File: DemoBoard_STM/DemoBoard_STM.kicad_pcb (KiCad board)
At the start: 4 copper layers, 45 x 45 mm, 57 parts, among them J1 USB4110GFA, J6 M55-7101242R, J7 MSD-1-A, J8 Conn_01x17_Pin, SW1 SW_Push, SW2 SW_Push, U1 RP2040, U2 W25Q128JVSIM, U3 MCP2518FDT-E_QBB, U4 TCAN332DCNR, U5 TLV75533PDBVR, Y1 ABM8-272-T3, Y2 ABM8-20.000MHZ-10-B1U-T

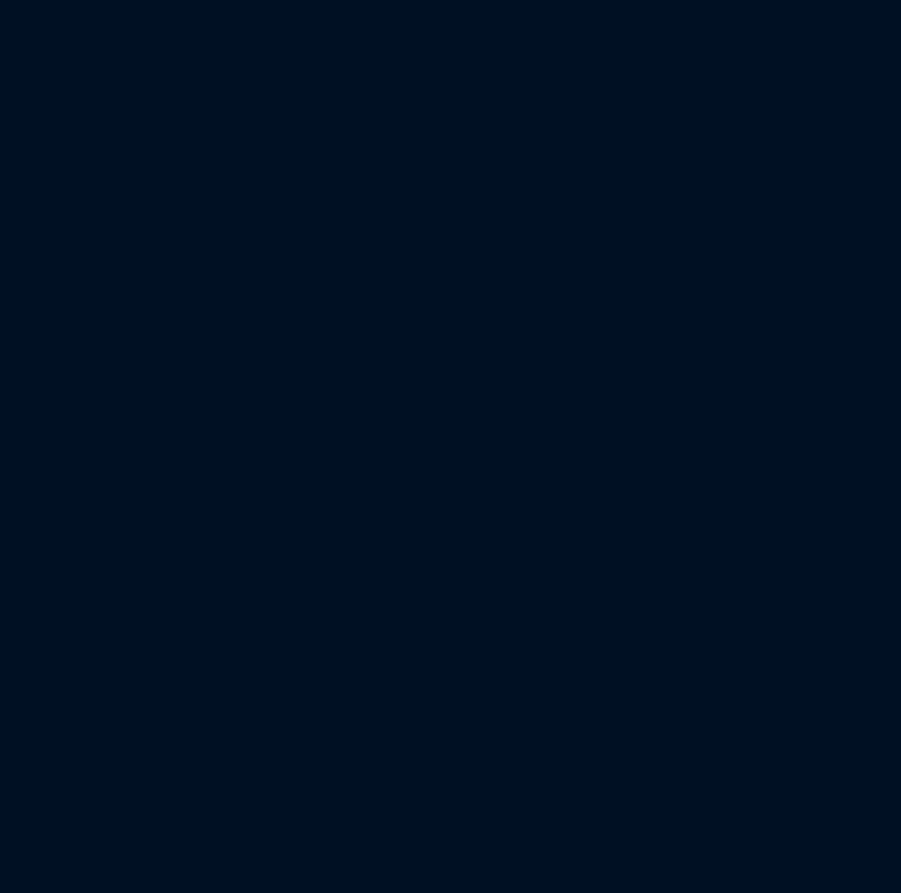
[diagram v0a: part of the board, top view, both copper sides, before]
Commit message: schematic_added_flash
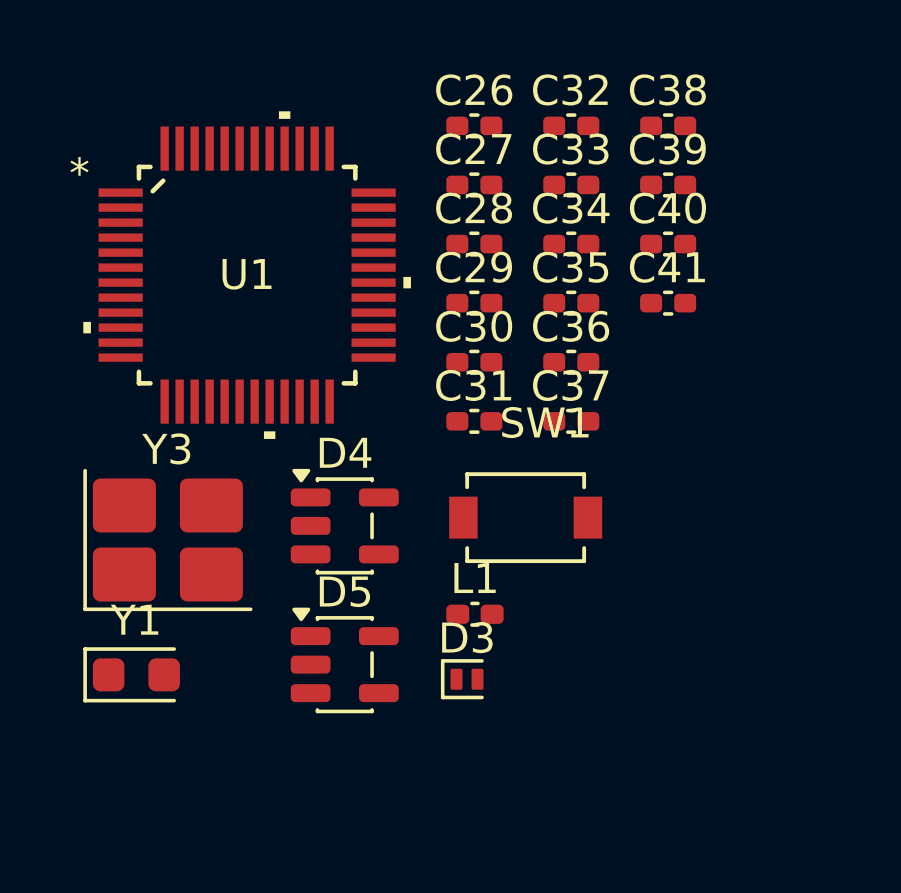
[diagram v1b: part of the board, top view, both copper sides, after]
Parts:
- added C26: 1uF, Capacitor_SMD:C_0402_1005Metric_Pad0.74x0.62mm_HandSolder, F.Cu at (13.0, 0.48)
- added C27: 100nF, Capacitor_SMD:C_0402_1005Metric_Pad0.74x0.62mm_HandSolder, F.Cu at (13.0, 2.46)
- added C28: 100nF, Capacitor_SMD:C_0402_1005Metric_Pad0.74x0.62mm_HandSolder, F.Cu at (13.0, 4.42)
- added C29: 100nF, Capacitor_SMD:C_0402_1005Metric_Pad0.74x0.62mm_HandSolder, F.Cu at (13.0, 6.39)
- added C30: 10uF, Capacitor_SMD:C_0402_1005Metric_Pad0.74x0.62mm_HandSolder, F.Cu at (13.0, 8.37)
- added C31: 100nF, Capacitor_SMD:C_0402_1005Metric_Pad0.74x0.62mm_HandSolder, F.Cu at (13.0, 10.3)
- added C32: 10uF, Capacitor_SMD:C_0402_1005Metric_Pad0.74x0.62mm_HandSolder, F.Cu at (16.3, 0.48)
- added C33: 2.2uF, Capacitor_SMD:C_0402_1005Metric_Pad0.74x0.62mm_HandSolder, F.Cu at (16.3, 2.46)
- added C34: 2.2uF, Capacitor_SMD:C_0402_1005Metric_Pad0.74x0.62mm_HandSolder, F.Cu at (16.3, 4.42)
- added C35: 6.8pF, Capacitor_SMD:C_0402_1005Metric_Pad0.74x0.62mm_HandSolder, F.Cu at (16.3, 6.39)
- added C36: 6.8pF, Capacitor_SMD:C_0402_1005Metric_Pad0.74x0.62mm_HandSolder, F.Cu at (16.3, 8.37)
- added C37: 12pF, Capacitor_SMD:C_0402_1005Metric_Pad0.74x0.62mm_HandSolder, F.Cu at (16.3, 10.3)
- added C38: 12pF, Capacitor_SMD:C_0402_1005Metric_Pad0.74x0.62mm_HandSolder, F.Cu at (19.5, 0.48)
- added C39: 100nF, Capacitor_SMD:C_0402_1005Metric_Pad0.74x0.62mm_HandSolder, F.Cu at (19.5, 2.46)
- added C40: 1uF, Capacitor_SMD:C_0402_1005Metric_Pad0.74x0.62mm_HandSolder, F.Cu at (19.5, 4.42)
- added C41: 100nF, Capacitor_SMD:C_0402_1005Metric_Pad0.74x0.62mm_HandSolder, F.Cu at (19.5, 6.39)
- added D3: PESD3V3U1UL, Diode_SMD:D_SOD-882, F.Cu at (12.8, 18.9)
- added D4: ESDA14V2SC5, Package_TO_SOT_SMD:SOT-23-5, F.Cu at (8.71, 13.8)
- added D5: ESDA14V2SC5, Package_TO_SOT_SMD:SOT-23-5, F.Cu at (8.71, 18.4)
- added L1: 2.2uH, Inductor_SMD:L_0402_1005Metric_Pad0.77x0.64mm_HandSolder, F.Cu at (13.1, 16.8)
- added SW1: SW_Push, inspireFly:SW_TL1015AF160QG, F.Cu at (14.7, 13.5)
- added U1: STM32U375CGT6Q, inspireFly:LQFP48_STM, F.Cu at (5.46, 5.46)
- added Y1: 32.768kHz, Crystal:Crystal_SMD_2012-2Pin_2.0x1.2mm_HandSoldering, F.Cu at (1.77, 18.8)
- added Y3: 16MHz, Crystal:Crystal_SMD_3225-4Pin_3.2x2.5mm_HandSoldering, F.Cu at (2.82, 14.3)

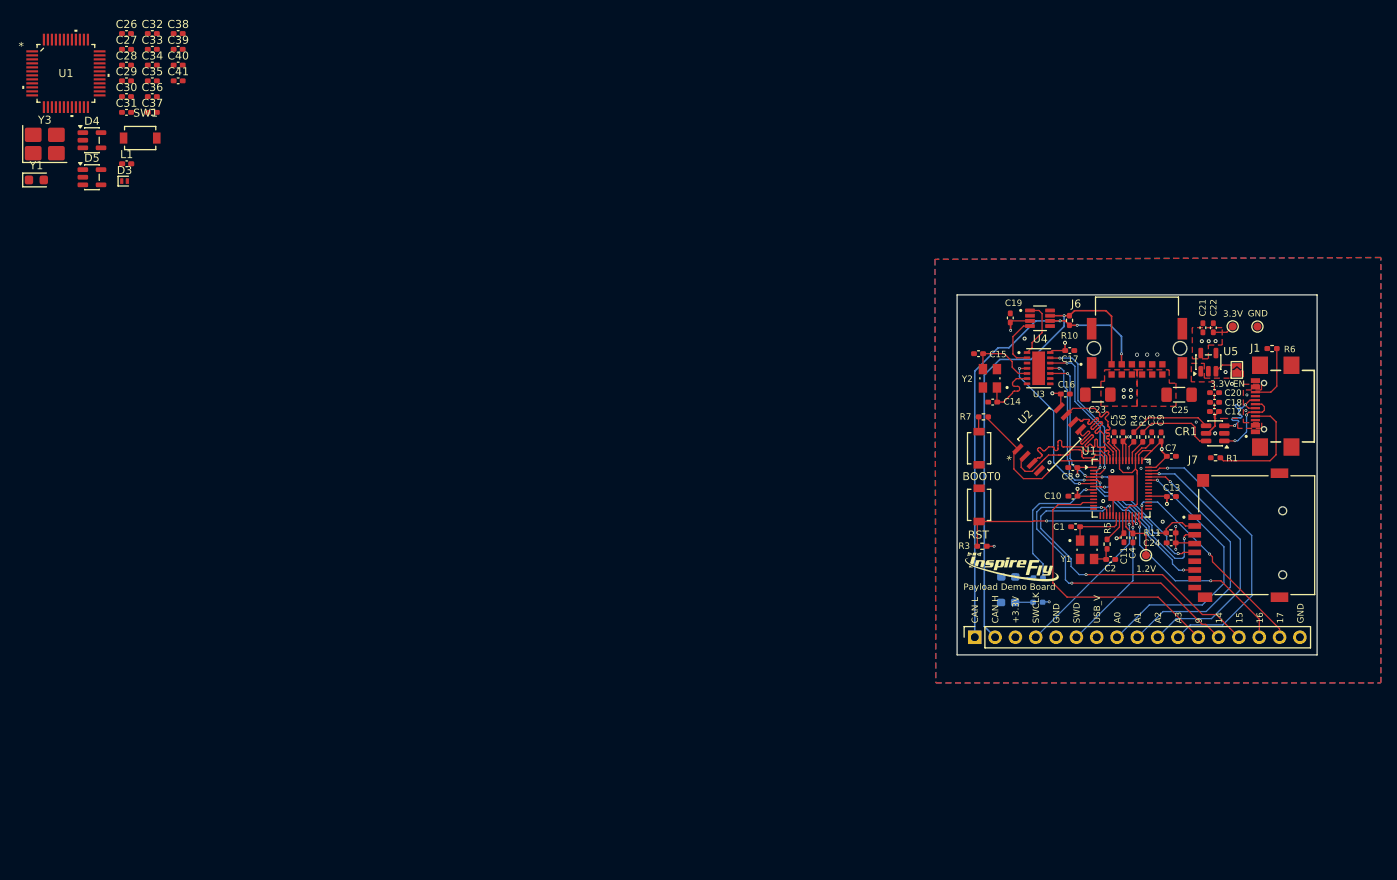
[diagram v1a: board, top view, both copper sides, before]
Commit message: Routing + schematic updates for STM
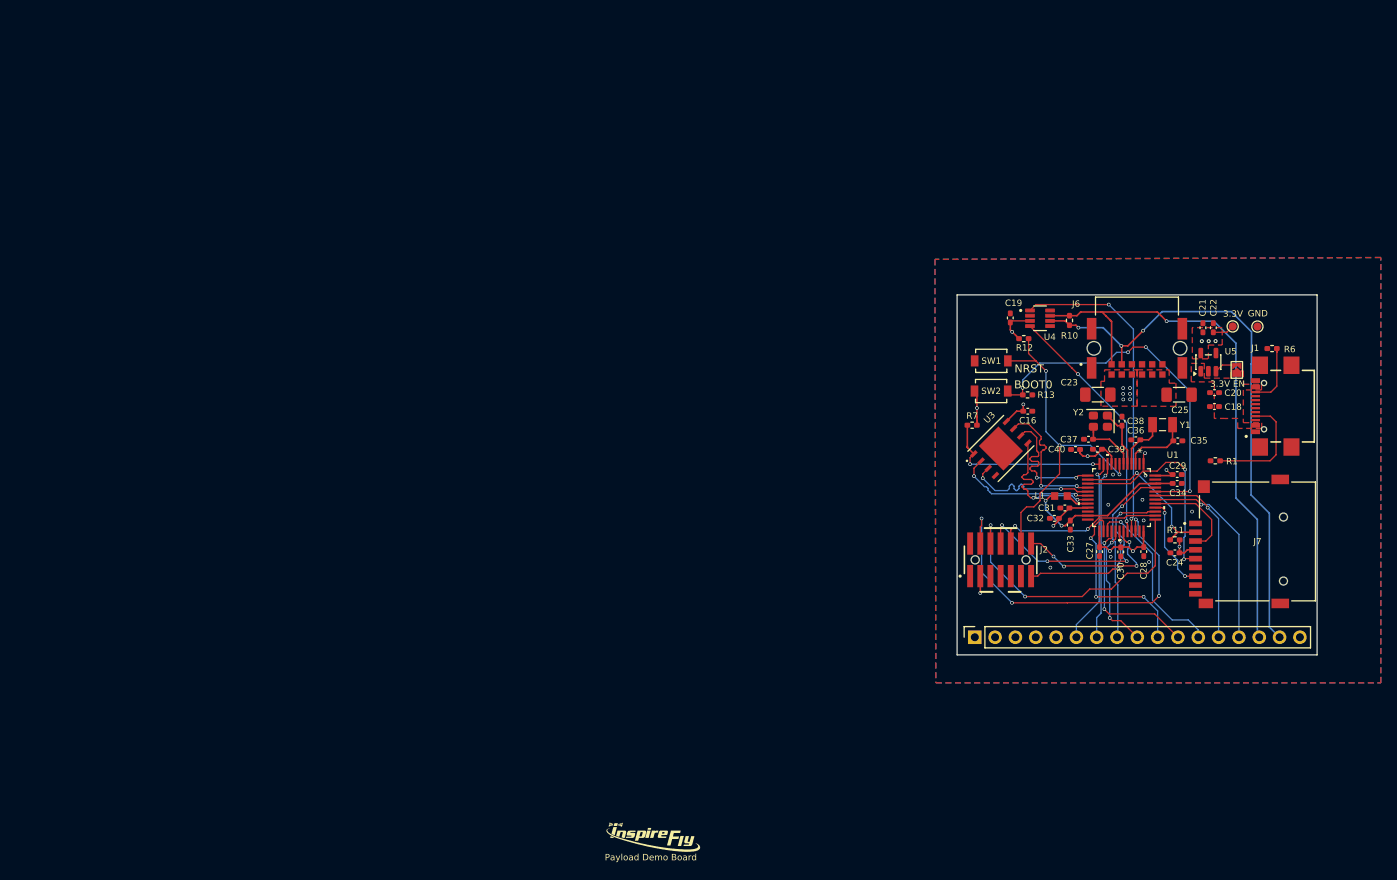
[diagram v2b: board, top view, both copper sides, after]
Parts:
- removed C1, C2: 15pF, Capacitor_SMD:C_0402_1005Metric_Pad0.74x0.62mm_HandSolder
- removed C10, C11, C12, C13, C17, C4, C41, C5, C6, C7, C8: 100nF, Capacitor_SMD:C_0402_1005Metric_Pad0.74x0.62mm_HandSolder
- removed C14, C15: 18pF, Capacitor_SMD:C_0402_1005Metric_Pad0.74x0.62mm_HandSolder
- removed C26, C3, C9: 1uF, Capacitor_SMD:C_0402_1005Metric_Pad0.74x0.62mm_HandSolder
- removed CR1: USBLC6-2SC6, Package_TO_SOT_SMD:SOT-23-6
- removed D1: LTST-C190KSKT, LED_SMD:LED_0603_1608Metric_Pad1.05x0.95mm_HandSolder
- removed D2: LTST-S270KRKT, LED_SMD:LED_0603_1608Metric_Pad1.05x0.95mm_HandSolder
- removed D3: PESD3V3U1UL, Diode_SMD:D_SOD-882
- removed D4, D5: ESDA14V2SC5, Package_TO_SOT_SMD:SOT-23-5
- removed R2, R4: 27.4, Resistor_SMD:R_0402_1005Metric_Pad0.72x0.64mm_HandSolder
- removed R3: 10k, Resistor_SMD:R_0402_1005Metric_Pad0.72x0.64mm_HandSolder
- removed R5, R8, R9: 1k, Resistor_SMD:R_0402_1005Metric_Pad0.72x0.64mm_HandSolder
- removed the SW1 at (14.7, 13.5)
- removed the SW1 at (119.6, 59.4)
- removed TP1: 1.2V, TestPoint:TestPoint_Pad_D1.0mm
- removed the U1 at (137.4, 57.3)
- removed the U1 at (5.46, 5.46)
- removed U2: W25Q128JVSIM, inspireFly:SOIC_128JVSIM_WIN
- removed the Y1 at (133.1, 65.0)
- removed the Y1 at (1.77, 18.8)
- removed Y3: 16MHz, Crystal:Crystal_SMD_3225-4Pin_3.2x2.5mm_HandSoldering
- added J2: Conn_ST_STDC14, inspireFly:SAMTEC_FTSH-107-01-L-DV-K-A, F.Cu at (122.3, 66.3)
- added R12: 10k, Resistor_SMD:R_0402_1005Metric_Pad0.72x0.64mm_HandSolder, F.Cu at (125.2, 38.6)
- added R13: 100k, Resistor_SMD:R_0402_1005Metric_Pad0.72x0.64mm_HandSolder, F.Cu at (125.7, 45.6)
- added SW1: SW_Push, inspireFly:SW_TL1015AF160QG, F.Cu at (121.1, 41.4)
- added U1: STM32U375CGT6Q, inspireFly:LQFP48_STM, F.Cu at (137.4, 58.5)
- added Y1: 32.768kHz, inspireFly:XTAL_ABS07-32.768KHZ-T, F.Cu at (142.5, 49.4)
- C35, C36: value 6.8pF -> 22pF
- C37, C38: value 12pF -> 18pF
- L1: footprint Inductor_SMD:L_0402_1005Metric_Pad0.77x0.64mm_HandSolder -> inspireFly:INDC1608X95N
- U3: value MCP2518FDT-E_QBB -> W25Q128JVPIQ TR; footprint inspireFly:SON65P450X300X90-15N -> inspireFly:WSON-8_6X5_WIN
- Y2: value ABM8-20.000MHZ-10-B1U-T -> 8Z-16.000MAHE-T; footprint inspireFly:XTAL_ABM8-272-T3 -> Crystal:Crystal_SMD_2520-4Pin_2.5x2.0mm
- moved C28 141.0 mm to (140.2, 65.2), turned to 90 degrees
- moved C29 140.3 mm to (144.4, 55.6), turned to 180 degrees
- moved C34 138.4 mm to (144.4, 56.7)
- moved C27 136.9 mm to (134.7, 65.2), turned to 90 degrees
- moved C30 136.7 mm to (137.3, 65.3), turned to 90 degrees
- moved C35 135.9 mm to (144.5, 51.4)
- moved C36 130.2 mm to (139.2, 51.3)
- moved C33 129.2 mm to (131.0, 61.9), turned to 90 degrees
- moved C32 128.0 mm to (129.0, 61.1), turned to 180 degrees
- moved C38 127.5 mm to (137.5, 48.9), turned to -90 degrees
- moved C31 127.3 mm to (130.3, 59.8)
- moved C39 125.3 mm to (134.4, 52.4), turned to 180 degrees
- moved L1 123.9 mm to (129.8, 58.3), turned to 180 degrees
- moved C37 123.9 mm to (133.3, 51.2), turned to 180 degrees
- moved C40 122.0 mm to (131.7, 52.5), turned to 180 degrees
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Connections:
- net Net-(C33-Pad2) renamed +1.1V
- net SPI0_CS_SDCARD renamed SPI1_CS_SDCARD
- C27 pad 2: VDD -> +3.3V
- C28 pad 2: VDD -> +3.3V
- C29 pad 2: VDD -> +3.3V
- C30 pad 2: VDD -> +3.3V
- C31 pad 2: VDD -> +3.3V
- C32 pad 1: VDD -> +3.3V
- C38 pad 1: Net-(U1-PH0-OSC_IN) -> GND
- C38 pad 2: GND -> Net-(U1-PH0-OSC_IN)
- C39 pad 1: VDDA -> +3.3V
- C40 pad 1: VDDA -> +3.3V
- J1 pad A6: Net-(J1-DP1) -> unconnected-(J1-DP1-PadA6)
- J1 pad A7: Net-(J1-DN1) -> unconnected-(J1-DN1-PadA7)
- J1 pad B6: Net-(J1-DP1) -> unconnected-(J1-DP2-PadB6)
- J1 pad B7: Net-(J1-DN1) -> unconnected-(J1-DN2-PadB7)
- J7 pad 3: SPI0_MOSI -> SPI1_MOSI
- J7 pad 5: SPI0_CLK -> SPI1_CLK
- J7 pad 7: SPI0_MISO -> SPI1_MISO
- J8 pad 1: CAN_LOW -> +3.3V
- J8 pad 10: ADC_2 -> SPI2_CLK
- J8 pad 11: ADC_3 -> SPI2_MOSI
- J8 pad 12: GPIO_9 -> SPI2_MISO
- J8 pad 13: GPIO_14 -> I2C1_SDA
- J8 pad 14: GPIO_15 -> I2C1_SCL
- J8 pad 15: GPIO_16 -> CAN_HIGH
- J8 pad 16: GPIO_17 -> CAN_LOW
- J8 pad 2: CAN_HIGH -> +3.3V
- J8 pad 3: +3.3V -> GND
- J8 pad 4: SWCLK -> GND
- J8 pad 6: SWD -> ADC1_IN4
- J8 pad 7: USB_VOLTAGE -> ADC1_IN3
- J8 pad 8: ADC_0 -> SPI2_CS1
- J8 pad 9: ADC_1 -> SPI2_CS2
- R7 pad 2: Net-(R7-Pad2) -> +3.3V
- SW2 pad 1: GND -> PH3-BOOT0
- SW2 pad 2: Net-(R7-Pad2) -> +3.3V
- U3 pad 1: Net-(U3-TXCAN) -> QSPI_CS
- U3 pad 2: Net-(U3-RXCAN) -> QSPI_SD1
- U3 pad 3: unconnected-(U3-CLKO/SOF-Pad3) -> QSPI_SD2
- U3 pad 4: INT_CAN_CONTROLLER -> GND
- U3 pad 5: Net-(U3-OSC2) -> QSPI_SD0
- U3 pad 6: Net-(U3-OSC1) -> QSPI_CLK
- U3 pad 7: GND -> QSPI_SD3
- U3 pad 8: unconnected-(U3-~{INT1}/GPIO1-Pad8) -> +3.3V
- U3 pad 9: unconnected-(U3-~{INT0}/GPIO0/XSTBY-Pad9) -> GND
- U4 pad 1: Net-(U3-TXCAN) -> CAN_TX
- U4 pad 4: Net-(U3-RXCAN) -> CAN_RX
- Y2 pad 1: Net-(U3-OSC1) -> Net-(U1-PH0-OSC_IN)
- Y2 pad 3: Net-(U3-OSC2) -> Net-(U1-PH1-OSC_OUT)
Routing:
- net USB_VOLTAGE: track 53.2 -> 0.00 mm, vias 1 -> 0
- net JTMS/SWDIO: track 0.00 -> 47.5 mm, vias 0 -> 4
- net PH3-BOOT0: track 0.00 -> 45.7 mm, vias 0 -> 4
- net NRST: track 0.00 -> 44.5 mm, vias 0 -> 3
- net GPIO_15: track 42.9 -> 0.00 mm, vias 2 -> 0
- net GPIO_14: track 41.9 -> 0.00 mm, vias 2 -> 0
- net CAN_TX: track 0.00 -> 40.9 mm, vias 0 -> 2
- net SPI0_MOSI: track 38.6 -> 0.00 mm, vias 4 -> 0
- net SPI0_MISO: track 38.2 -> 0.00 mm, vias 3 -> 0
- net JTCK/SWCLK: track 0.00 -> 36.6 mm, vias 0 -> 2
- net GPIO_9: track 35.6 -> 0.00 mm
- net ADC_3: track 35.5 -> 0.00 mm, vias 1 -> 0
- net SPI0_CLK: track 34.7 -> 0.00 mm, vias 4 -> 0
- net ADC_2: track 34.0 -> 0.00 mm, vias 1 -> 0
- net ADC_0: track 33.8 -> 0.00 mm, vias 1 -> 0
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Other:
- board text added: "+3.3V +3.3V +3.3V GND GND PA0 / ADC1_IN3 PA1 / ADC1_IN4 PB8 / SPI2_CS1 PA8 / SPI2_CS2 PB13 / SPI2_CLK PB15 / SPI2_MOSI PB14 / SPI2_MISO PB7 / I2C1_SDA PB6 / I2C1_SCL CAN HI CAN LO GND"
- board text added: "NRST"
- board text removed: "CAN L CAN H +3.3V SWCLK GND SWD USB_V A0 A1 A2 A3 9 14 15 16 17 GND"
- board text removed: "RST"

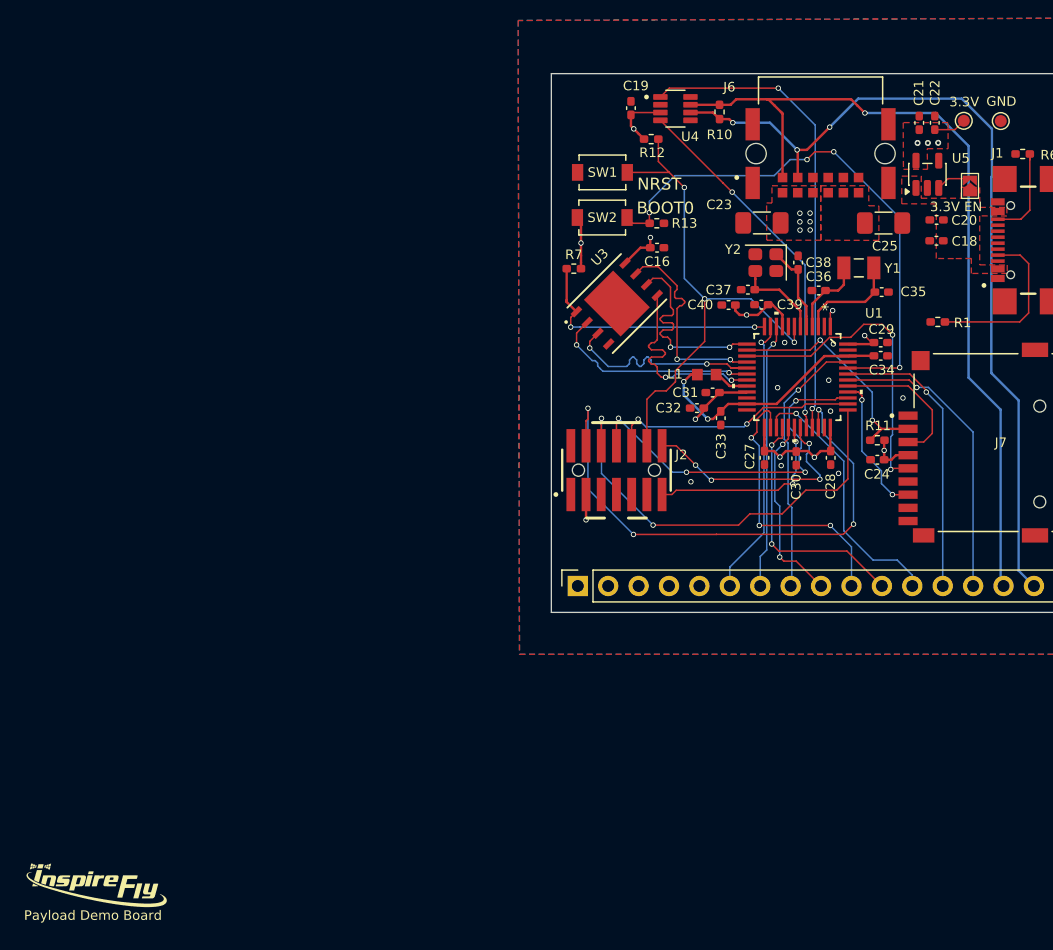
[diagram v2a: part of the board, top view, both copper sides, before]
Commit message: Finalize STM payload + BOM
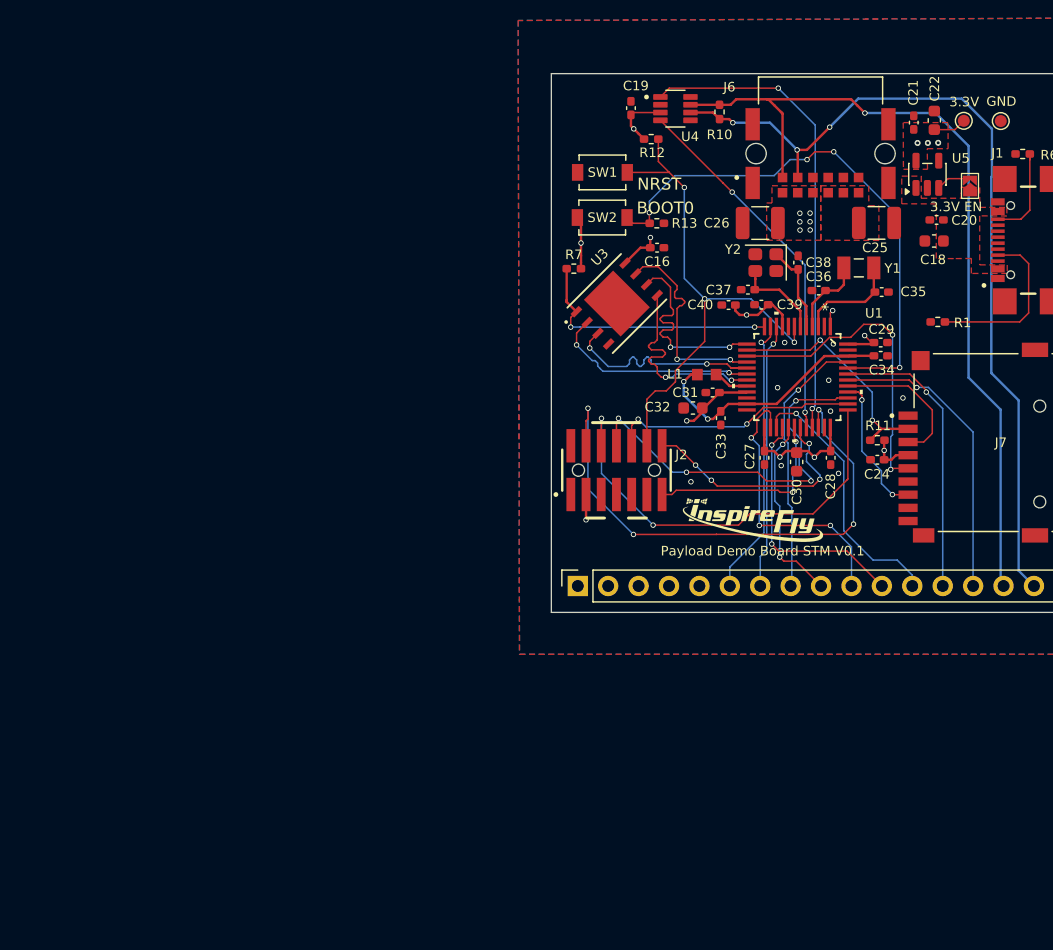
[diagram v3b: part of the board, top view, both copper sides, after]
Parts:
- removed C23: 47uF, Capacitor_SMD:C_1206_3216Metric_Pad1.33x1.80mm_HandSolder
- added C26: 22uF, Capacitor_SMD:C_1210_3225Metric, F.Cu at (134.3, 45.6)
- C18, C22, C30, C32: footprint Capacitor_SMD:C_0402_1005Metric_Pad0.74x0.62mm_HandSolder -> Capacitor_SMD:C_0603_1608Metric
- C25: value 47uF -> 22uF; footprint Capacitor_SMD:C_1206_3216Metric_Pad1.33x1.80mm_HandSolder -> Capacitor_SMD:C_1210_3225Metric
- moved G*** 62.7 mm to (133.7, 70.4)
- moved C25 0.59 mm to (144.0, 45.6)
- moved C21 0.46 mm to (147.1, 37.2)
- moved C32 0.33 mm to (128.7, 61.1)
- moved C30 0.30 mm to (137.3, 65.6)
- moved C22 0.21 mm to (148.8, 37.0)
- moved C18 0.20 mm to (148.8, 47.1)
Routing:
- net SWO: track 31.2 -> 32.9 mm
- net +3.3V: track 56.5 -> 57.3 mm
- net DEBUG_LPUART_TX: track 16.6 -> 17.2 mm
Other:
- board text added: "Payload Demo Board STM V0.1"
- board text removed: "Payload Demo Board"
